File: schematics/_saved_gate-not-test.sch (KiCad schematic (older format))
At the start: 2 parts

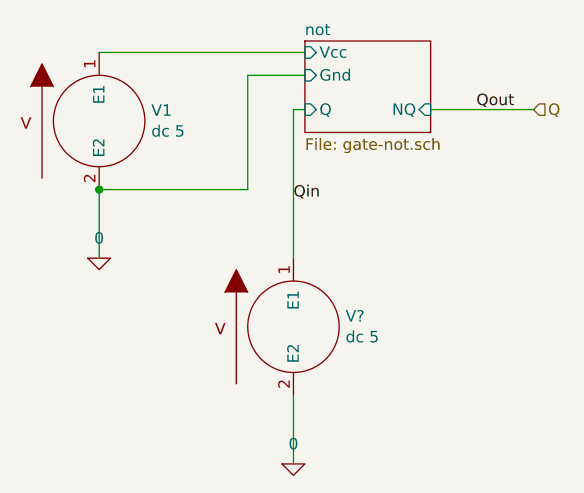
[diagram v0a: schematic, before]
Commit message: Adds a primitive directory iterator
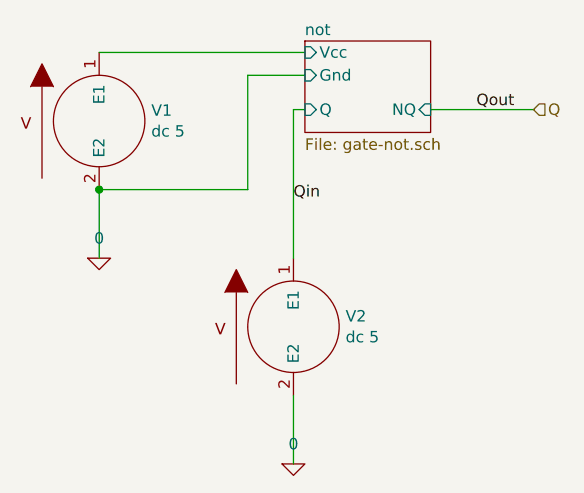
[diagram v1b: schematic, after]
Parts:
- gave numbers to parts that had none: 1
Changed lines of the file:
@@
 	3650 3400 4550 3400
 $Comp
-L pspice:0 #GND?
+L pspice:0 #GND02
 U 1 1 5C568E4F
 P 4500 5200
-F 0 "#GND?" H 4500 5100 50  0001 C CNN
+F 0 "#GND02" H 4500 5100 50  0001 C CNN
 F 1 "0" H 4500 5287 50  0000 C CNN
 F 2 "" H 4500 5200 50  0001 C CNN
@@
 $EndComp
 $Comp
-L pspice:VSOURCE V?
+L pspice:VSOURCE V2
 U 1 1 5C568E55
 P 4500 4600
-F 0 "V?" H 4728 4646 50  0000 L CNN
+F 0 "V2" H 4728 4646 50  0000 L CNN
 F 1 "dc 5" H 4728 4555 50  0000 L CNN
 F 2 "" H 4500 4600 50  0001 C CNN
